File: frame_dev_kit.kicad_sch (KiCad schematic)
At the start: 76 parts, among them J1 FR02C051JA1-R5000, J2 SWD, J3 UART Out, J4 Battery 2, J5 Battery 1, J6 Conn_01x03, U1 MAX77654BENV+T, U2 ICS-41351, U3 MDBT50Q-1MV2, U4 GLF73910-BD01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

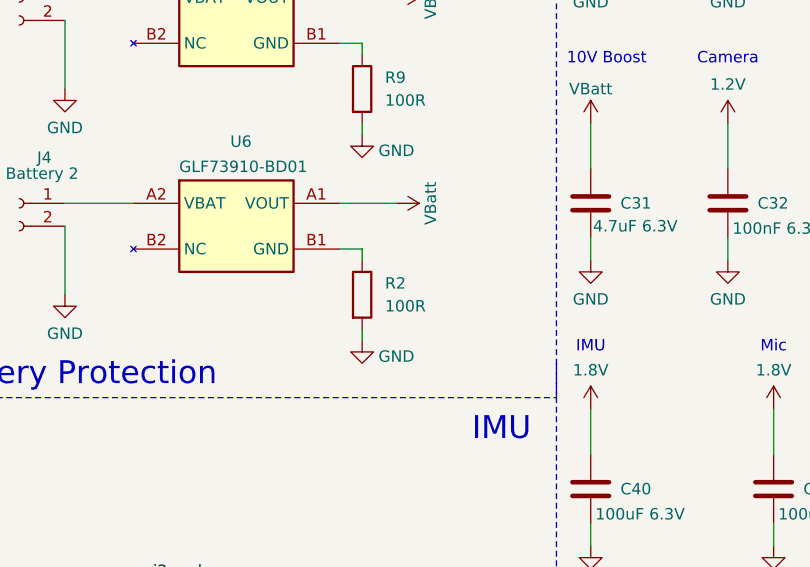
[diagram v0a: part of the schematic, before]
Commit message: fix duplicated R2
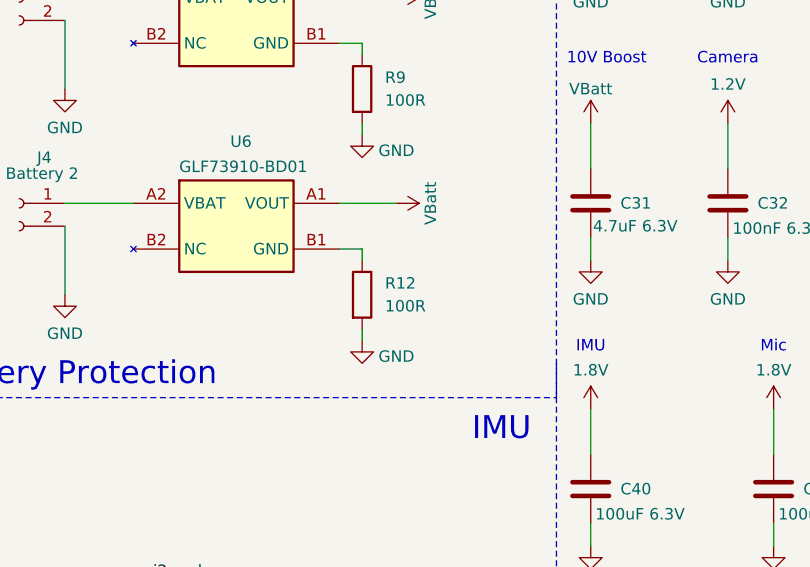
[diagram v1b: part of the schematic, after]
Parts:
- renumbered R2 to R12
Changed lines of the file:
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@@
 		(dnp no)
 		(fields_autoplaced yes)
-		(property "Reference" "R2"
+		(property "Reference" "R12"
 			(at 279.4 203.1999 0)
 			(effects
@@
 			(project "frame_dev_kit"
 				(path "/f8f60d15-ff2b-4c2a-8012-79eadce4ce58"
-					(reference "R2")
+					(reference "R12")
 					(unit 1)
 				)
